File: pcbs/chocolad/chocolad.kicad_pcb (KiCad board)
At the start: 2 copper layers, 110.5 x 87.9 mm, 75 parts, among them J1 TRRS, J2 OLED, SW1 SW_PUSH, SW10 SW_PUSH, SW11 SW_PUSH, SW12 SW_PUSH, SW13 SW_PUSH, SW14 SW_PUSH, SW15 SW_PUSH, SW16 SW_PUSH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

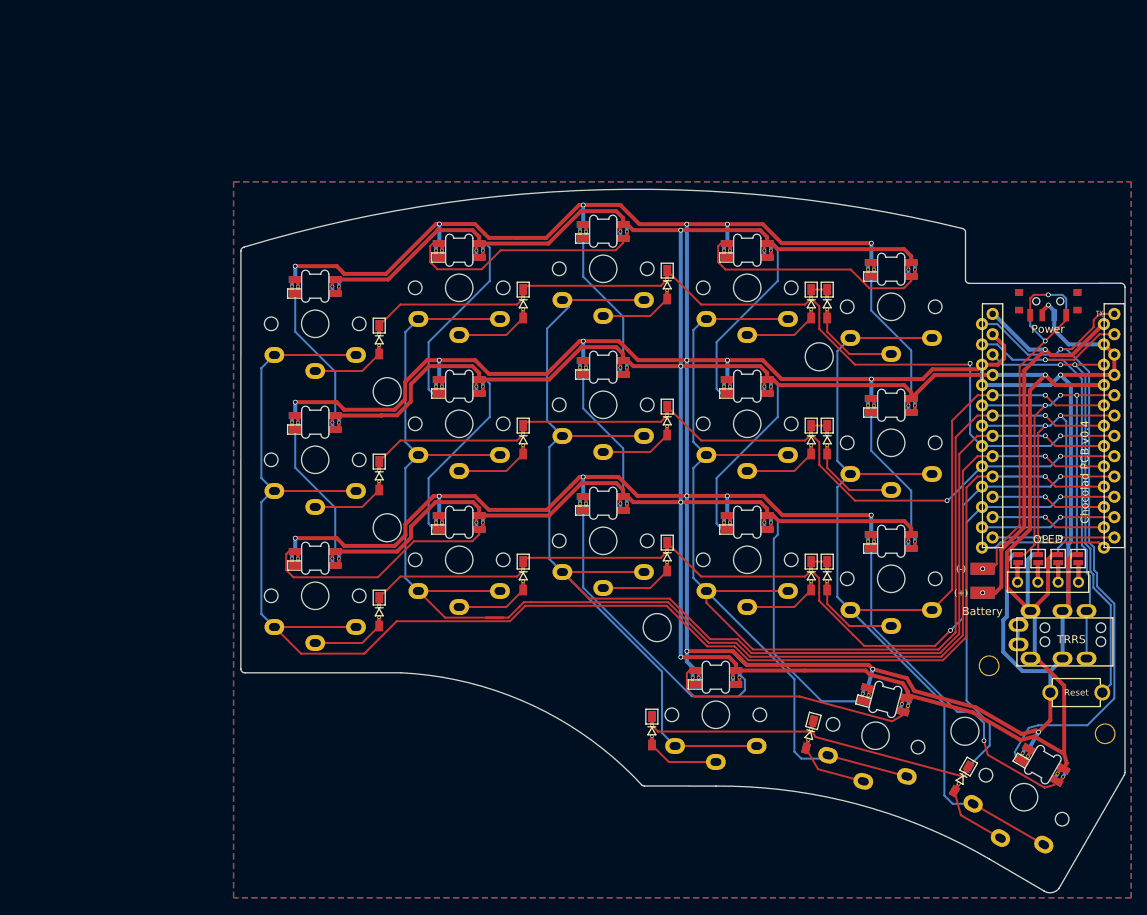
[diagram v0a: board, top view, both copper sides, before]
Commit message: Updated the sk6812 and battery pad footprints.
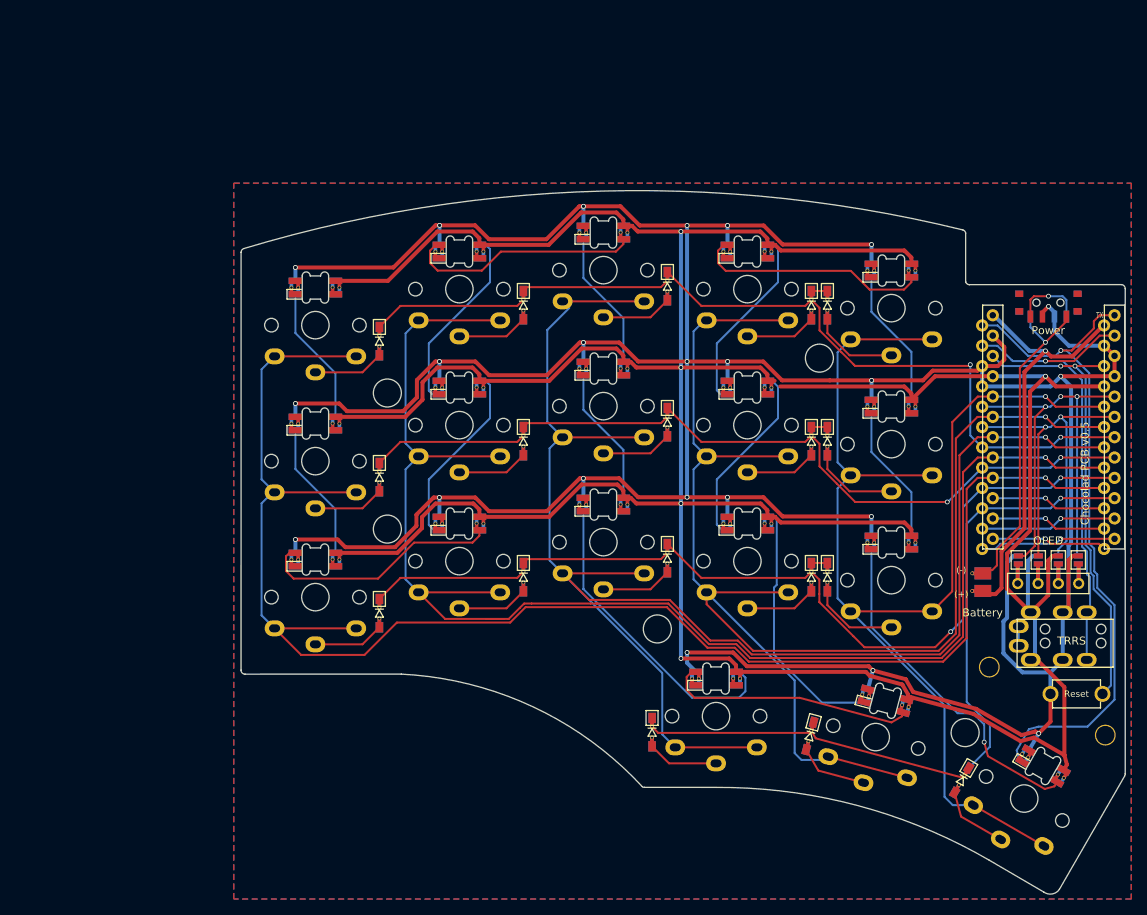
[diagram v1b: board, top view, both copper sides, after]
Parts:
- BT1: footprint chocolad:Battery_pads -> jmnw:Battery_pads_reversible_2
- L1, L10, L11, L12, L13, L14, L15, L16, L17, L18, L2, L3, L4, L5, L6, L7, L8, L9: footprint chocolad:SK6812_Mini_E -> jmnw:SK6812_Mini_E_edit
- moved SW4 0.17 mm to (119.3, 73.6)
- moved SW3 0.17 mm to (101.3, 71.3)
- moved JP2 0.17 mm to (158.2, 107.5)
- moved JP6 0.17 mm to (158.2, 107.5)
- moved SW7 0.17 mm to (83.3, 90.6)
- moved D14 0.17 mm to (127.3, 109.6)
- moved JP4 0.17 mm to (153.2, 107.5)
- moved JP8 0.17 mm to (153.2, 107.5)
- moved SW13 0.17 mm to (101.3, 105.3)
- moved SW2 0.17 mm to (83.3, 73.6)
- moved D11 0.17 mm to (73.3, 114.1)
- moved SW12 0.17 mm to (83.3, 107.6)
- moved SW14 0.17 mm to (119.3, 107.6)
- moved SW9 0.17 mm to (119.3, 90.6)
- moved D15 0.17 mm to (129.3, 109.6)
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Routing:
- net GND: track 518.1 -> 495.5 mm
- net VCC: track 451.6 -> 450.5 mm
- net Net-(BT1-Pad2): vias 2 -> 1
- net raw: vias 2 -> 1
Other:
- board text added: "Chocolad PCB v0.5"
- board text removed: "Chocolad PCB v0.4"

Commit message: Added and changed components and altered shape.
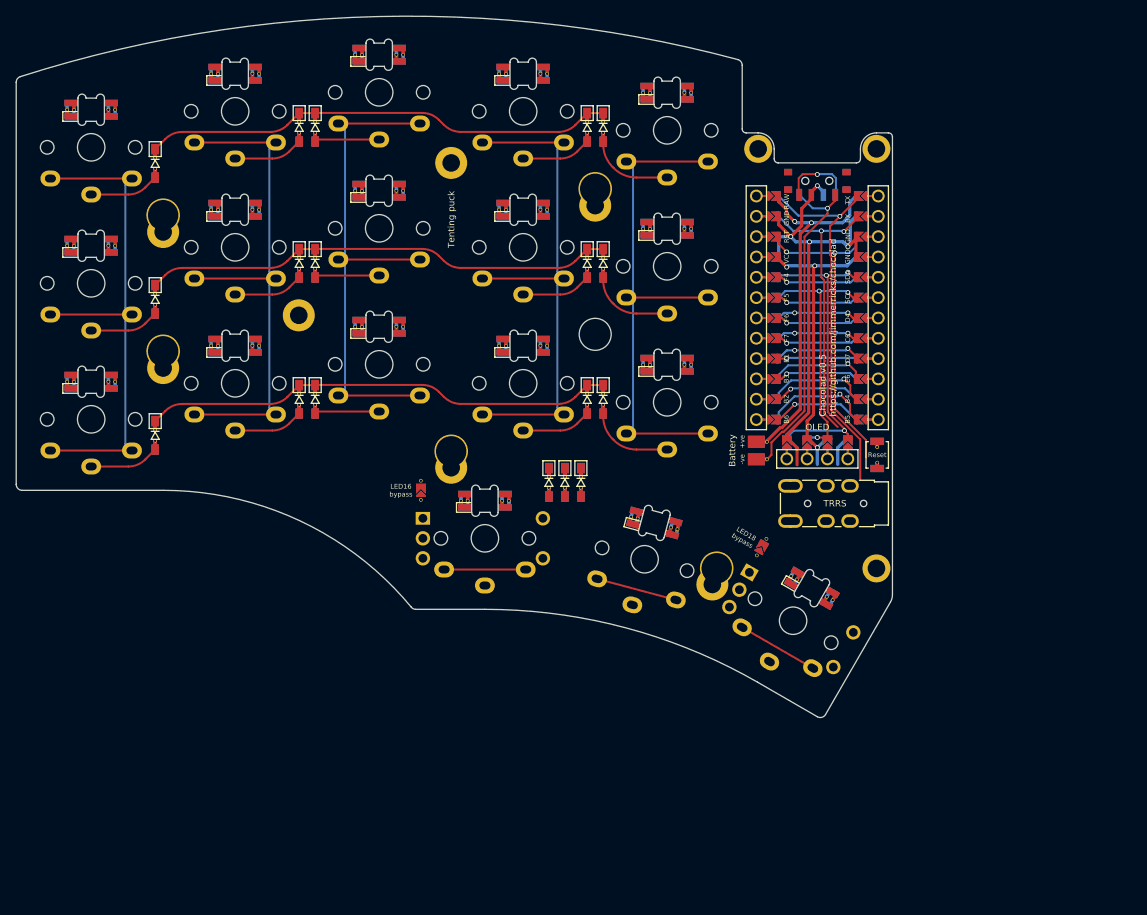
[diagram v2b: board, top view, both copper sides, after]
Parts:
- removed the ? at (149.6, 120.9)
- removed the ? at (164.1, 129.4)
- removed the ? at (74.3, 86.6)
- removed the ? at (74.3, 103.6)
- removed the ? at (128.3, 82.3)
- removed the ? at (146.5, 129.1)
- removed J2: OLED, chocolad:OLED
- removed JP3, JP4, JP5, JP6, JP7, JP8: , chocolad:Jumper
- removed RSW2: SW_SPDT, chocolad:Power
- added ?: , chocolad:M2_hole_3.5mm, F.Cu at (100.3, 79.3)
- added EN1: RotaryEncoder_Switch, swoop:RotaryEncoder, F.Cu at (86.5, 104.8)
- added EN2: RotaryEncoder_Switch, swoop:RotaryEncoder, F.Cu at (125.0, 115.1)
- added H2: M2 Hole, swoop:M2_double_hole_4mm, F.Cu at (46.3, 64.4)
- added H2: M2 Hole, swoop:M2_double_hole_4mm, F.Cu at (100.3, 61.1)
- added H2: M2 Hole, swoop:M2_double_hole_4mm, F.Cu at (46.3, 81.4)
- added H2: M2 Hole, swoop:M2_double_hole_4mm, F.Cu at (115.5, 108.5)
- added O1: OLED, swoop:OLED_jumpers, F.Cu at (124.2, 94.9)
- added PSW1: SW_SPDT, swoop:Power, F.Cu at (128.1, 60.1)
- added PUCK1: SYM_Arrow45_Small, swoop:Tenting_puck, F.Cu at (82.3, 76.9)
- added Ref**: Val**, swoop:M2_hole_3.5mm, F.Cu at (135.5, 108.6)
- added Ref**: Val**, swoop:M2_hole_3.5mm, F.Cu at (120.7, 56.1)
- added Ref**: Val**, swoop:M2_hole_3.5mm, F.Cu at (135.5, 56.1)
- ?: footprint chocolad:M2_hole_3.5mm -> jmnw:M2_hole_4.2mm
- BT1: footprint jmnw:Battery_pads_reversible_2 -> swoop:Battery_pads_reversible
- J1: footprint chocolad:TRRS_reversible -> swoop:TRRS-3pin
- JP1, JP2: value (none) -> LED bypass; footprint chocolad:Jumper -> swoop:Jumper
- RSW1: footprint chocolad:Reset -> swoop:Reset
- U1: footprint chocolad:ProMicro -> swoop:ProMicro_jumpers
- moved JP2 80.2 mm to (78.5, 98.8)
- moved D18 62.0 mm to (96.5, 97.8), turned to -90 degrees
- moved D8 48.3 mm to (65.3, 70.4)
- moved D3 48.3 mm to (65.3, 53.4)
- moved D13 48.3 mm to (65.3, 87.4)
- moved D17 42.7 mm to (98.5, 97.8), turned to -90 degrees
- moved JP1 39.6 mm to (121.1, 105.9), turned to -120 degrees
- moved RSW1 38.9 mm to (135.5, 94.4), turned to 90 degrees
- moved L16 36.5 mm to (86.5, 100.1)
- moved SW16 36.5 mm to (86.5, 104.8)
- moved SW18 36.5 mm to (125.0, 115.1)
- moved L17 36.5 mm to (107.7, 102.9)
- moved SW17 36.5 mm to (106.5, 107.4)
- moved L18 36.5 mm to (127.4, 111.0)
- moved ? 35.9 mm to (79.5, 94.4)
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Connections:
- net Net-(D16-Pad2) renamed er0
- net Net-(D18-Pad2) renamed er1
- J1 pad A: unconnected-(J1-PadA) -> VCC
- JP1 pad 1: GND -> LED
- JP1 pad 2: Net-(J2-Pad4) -> l15i
- JP2 pad 1: VCC -> l17o
- JP2 pad 2: Net-(J2-Pad3) -> l13i
- L13 pad 4: Net-(L13-Pad4) -> l13i
- L15 pad 4: Net-(L15-Pad4) -> l15i
- L16 pad 2: Net-(L13-Pad4) -> l13i
- L16 pad 4: Net-(L16-Pad4) -> l17o
- L17 pad 2: Net-(L16-Pad4) -> l17o
- L18 pad 2: Net-(L15-Pad4) -> l15i
- U1 pad 11: unconnected-(U1-Pad11) -> eda
- U1 pad 12: unconnected-(U1-Pad12) -> edb
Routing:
- net GND: track 495.5 -> 66.0 mm, vias 23 -> 4
- net VCC: track 450.5 -> 38.4 mm, vias 5 -> 3
- net col0: track 198.8 -> 75.7 mm
- net col2: track 203.7 -> 86.4 mm
- net col1: track 183.2 -> 76.2 mm
- net col3: track 187.8 -> 86.4 mm
- net row3: track 93.3 -> 12.1 mm
- net col4: track 155.1 -> 86.4 mm
- net row2: track 120.4 -> 70.0 mm
- net row0: track 113.0 -> 69.3 mm
- net Net-(L15-Pad4): track 43.0 -> 0.00 mm, vias 1 -> 0
- net Net-(L13-Pad4): track 39.1 -> 0.00 mm
- net LED: track 85.0 -> 47.1 mm
- net row1: track 105.3 -> 69.3 mm
- net Net-(L14-Pad2): track 32.1 -> 0.00 mm
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- removed copper zone on B.Cu, net (none)
- removed copper zone on F.Cu, net (none)
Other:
- board size 110.5 x 87.9 mm -> 109.5 x 87.7 mm
- board text added: "Chocolad v0.5 https://github.com/jimmerricks/chocolad"
- board text removed: "Battery"
- board text removed: "Chocolad PCB v0.5"
- board text removed: "OLED"
- board text removed: "Power"

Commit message: Finalised traces.
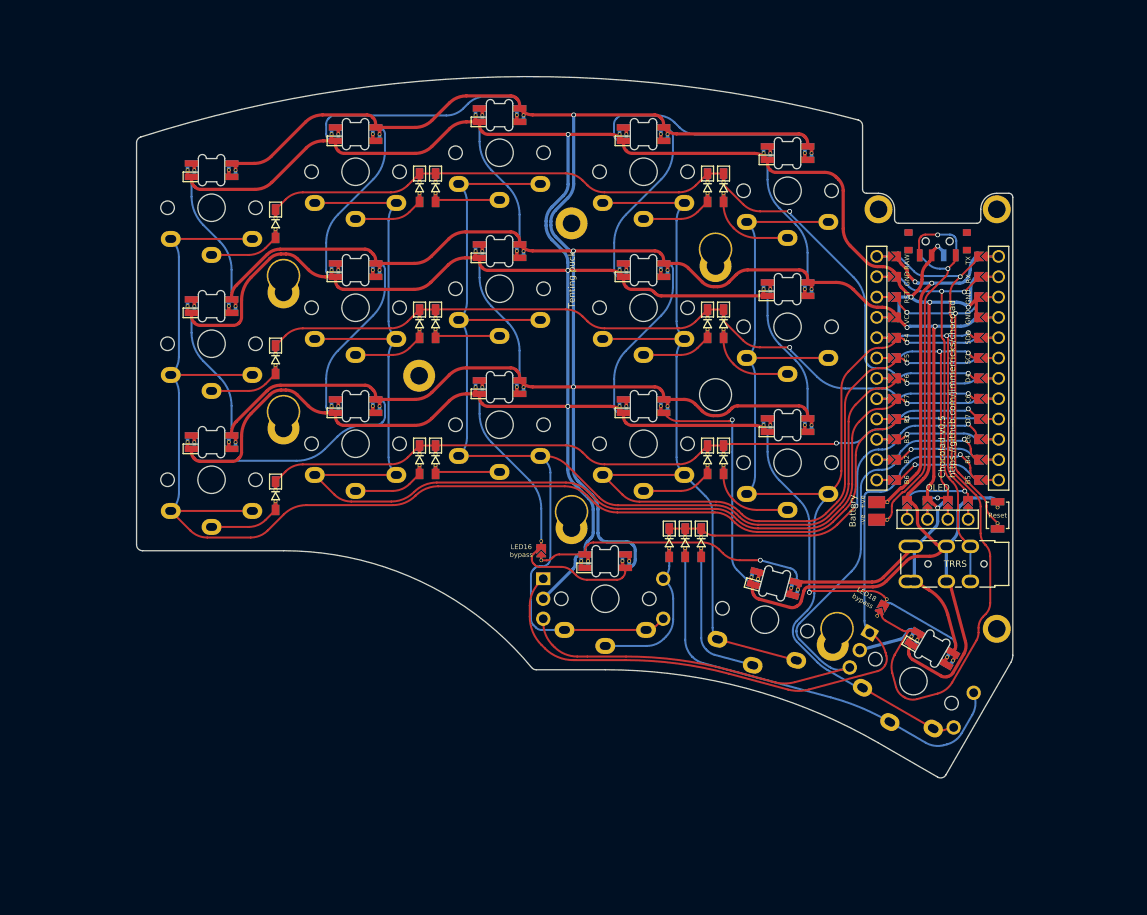
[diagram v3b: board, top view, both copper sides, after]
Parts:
- moved ? 19.2 mm to (97.3, 101.5)
- moved D17 16.8 mm to (113.6, 105.3)
- moved D5 16.8 mm to (116.3, 61.0)
- moved L5 16.8 mm to (124.3, 56.6)
- moved H2 16.8 mm to (61.3, 89.0)
- moved J1 16.8 mm to (150.4, 108.0)
- moved SW4 16.8 mm to (106.3, 59.0)
- moved SW8 16.8 mm to (88.3, 73.6)
- moved L4 16.8 mm to (106.3, 54.3)
- moved L17 16.8 mm to (122.7, 110.4)
- moved D16 16.8 mm to (109.6, 105.3)
- moved Ref** 16.8 mm to (135.7, 63.7)
- moved Ref** 16.8 mm to (150.5, 63.7)
- moved D4 16.8 mm to (114.3, 61.0)
- moved EN1 16.8 mm to (101.6, 112.3)
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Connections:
- U1 pad 11: eda -> edb
- U1 pad 12: edb -> eda
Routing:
- net GND: track 66.0 -> 478.8 mm, vias 4 -> 7
- net VCC: track 38.4 -> 396.6 mm, vias 3 -> 6
- net col0: track 75.7 -> 180.3 mm
- net col2: track 86.4 -> 176.7 mm
- net col1: track 76.2 -> 163.3 mm
- net eda: track 12.8 -> 94.1 mm
- net edb: track 13.5 -> 90.6 mm
- net col3: track 86.4 -> 161.9 mm
- net col4: track 86.4 -> 142.9 mm
- net er1: track 0.00 -> 54.6 mm
- net l15i: track 0.00 -> 44.7 mm, vias 0 -> 1
- net LED: track 47.1 -> 89.6 mm
- net l13i: track 0.00 -> 38.1 mm
- net row0: track 69.3 -> 107.4 mm
- net l17o: track 0.00 -> 36.8 mm, vias 0 -> 1
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
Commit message: Moved footprints into local library.
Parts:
- BT1: footprint swoop:Battery_pads_reversible -> chocolad:Battery_pads
- EN1, EN2: footprint swoop:RotaryEncoder -> chocolad:RotaryEncoder
- H1, H3, H5: renamed from H2; footprint swoop:M2_double_hole_4mm -> chocolad:M2_double_hole_4mm
- H2: footprint swoop:M2_double_hole_4mm -> chocolad:M2_double_hole_4mm
- H4: renamed from ?; footprint jmnw:M2_hole_4.2mm -> chocolad:M2_double_hole_4mm
- J1: footprint swoop:TRRS-3pin -> chocolad:TRRS
- JP1, JP2: footprint swoop:Jumper -> chocolad:Jumper
- L1: footprint jmnw:SK6812_Mini_E_edit -> chocolad:SK6812_Mini_E
- O1: footprint swoop:OLED_jumpers -> chocolad:OLED
- PSW1: footprint swoop:Power -> chocolad:Power
- PUCK1: footprint swoop:Tenting_puck -> chocolad:Tenting_puck
- RSW1: footprint swoop:Reset -> chocolad:Reset
- Ref** (x3): footprint swoop:M2_hole_3.5mm -> chocolad:M2_hole_3.5mm
- U1: footprint swoop:ProMicro_jumpers -> chocolad:ProMicro

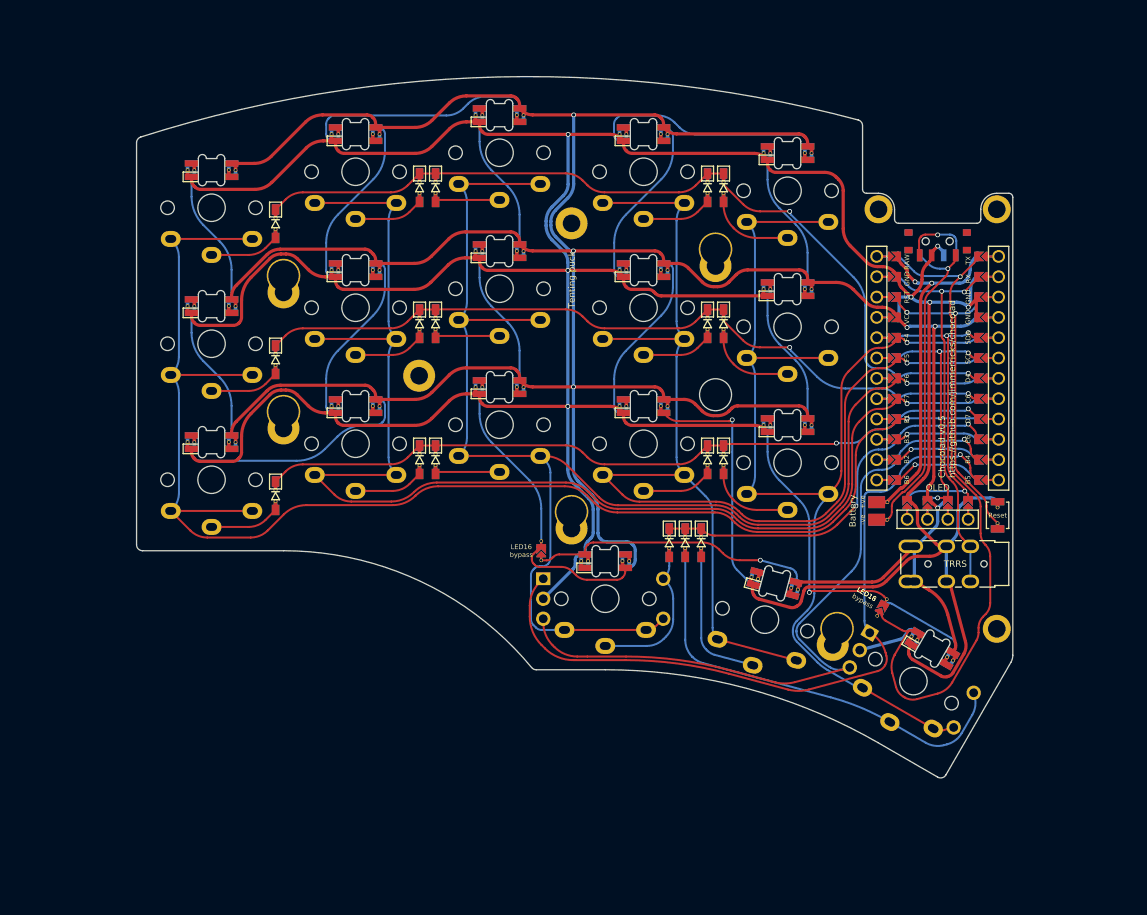
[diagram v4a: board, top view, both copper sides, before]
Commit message: Fixed the cover
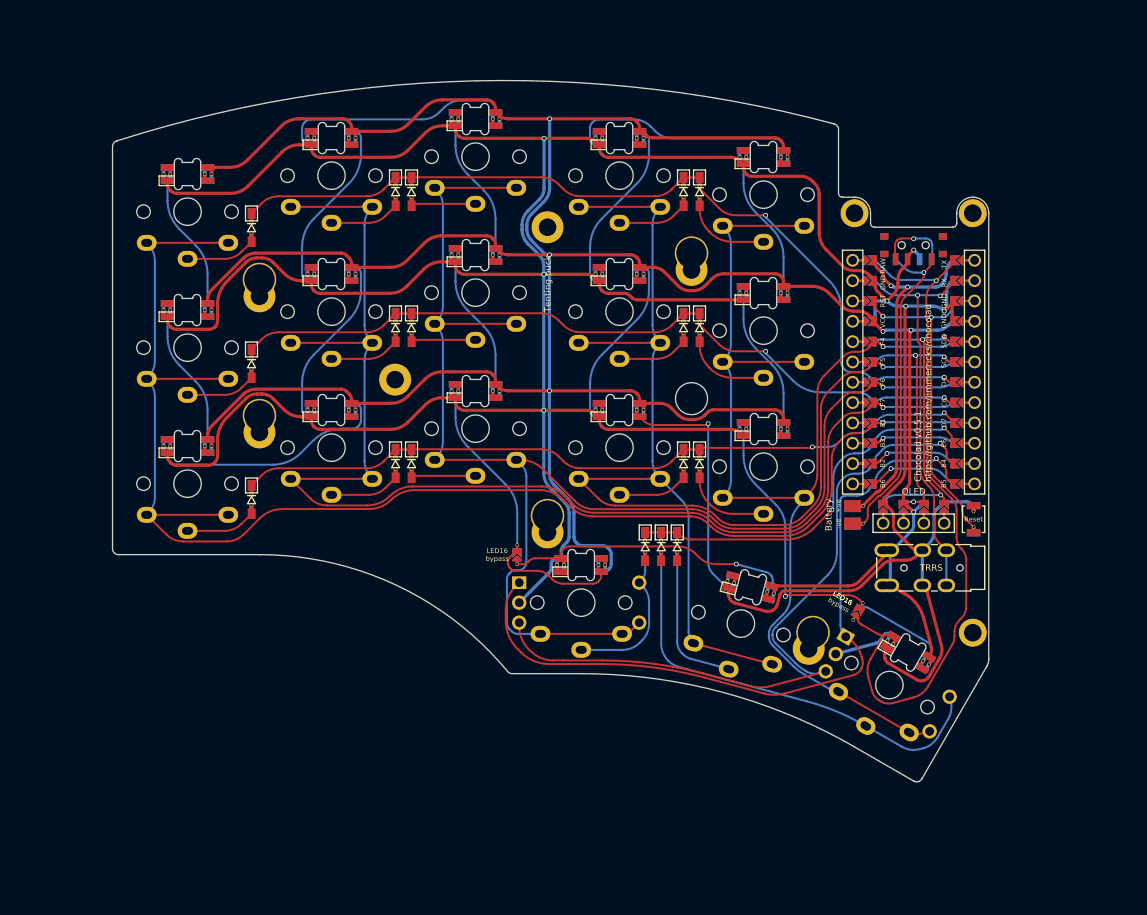
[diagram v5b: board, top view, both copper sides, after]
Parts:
- moved Ref** 3.04 mm to (147.5, 116.6)
- moved U1 3.04 mm to (140.1, 84.0)
- moved ? 3.04 mm to (112.3, 87.3)
- moved D15 3.04 mm to (113.3, 95.5)
- moved D16 3.04 mm to (106.5, 105.8)
- moved D18 3.04 mm to (108.5, 105.8)
- moved H2 3.04 mm to (58.3, 89.5)
- moved JP2 3.04 mm to (90.5, 106.8)
- moved L10 3.04 mm to (121.3, 74.1)
- moved L13 3.04 mm to (85.3, 86.4)
- moved L4 3.04 mm to (103.3, 54.8)
- moved L6 3.04 mm to (49.3, 76.3)
- moved L8 3.04 mm to (85.3, 69.4)
- moved SW10 3.04 mm to (121.3, 78.8)
- moved SW12 3.04 mm to (67.3, 93.5)
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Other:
- outline, holes or cut-outs redrawn
- board text added: "Chocolad v0.5.1 https://github.com/jimmerricks/chocolad"
- board text removed: "Chocolad v0.5 https://github.com/jimmerricks/chocolad"
